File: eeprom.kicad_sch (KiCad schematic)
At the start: 2 parts, among them U8 CAT25320VI-GT3

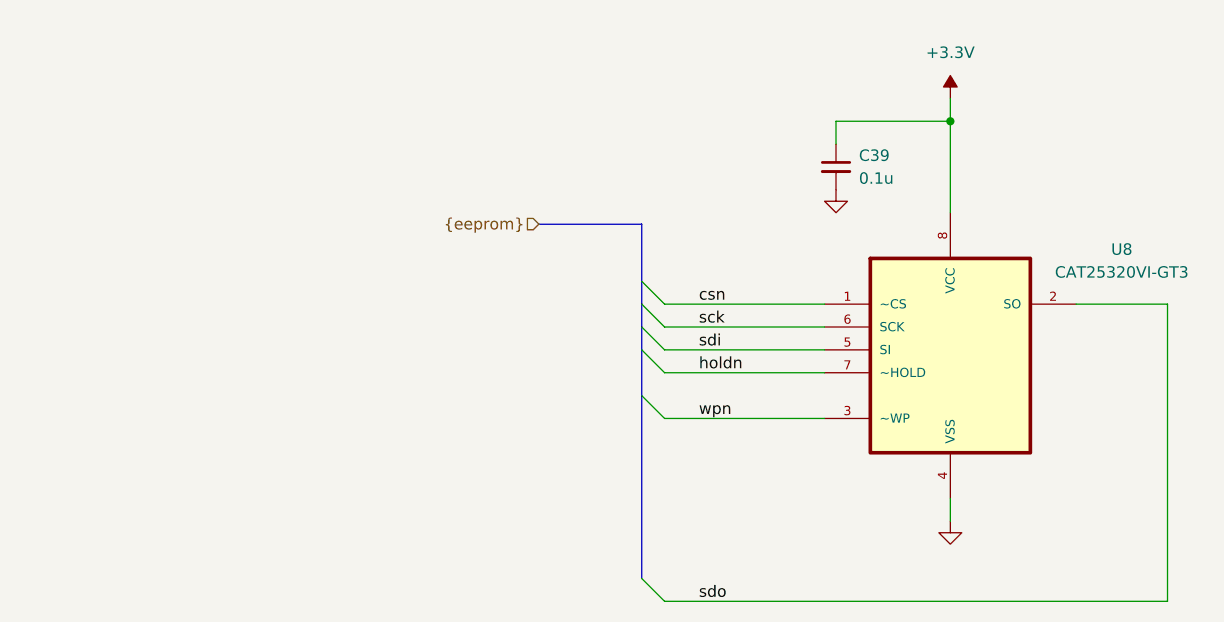
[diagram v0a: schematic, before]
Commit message: Add watchdog window IC
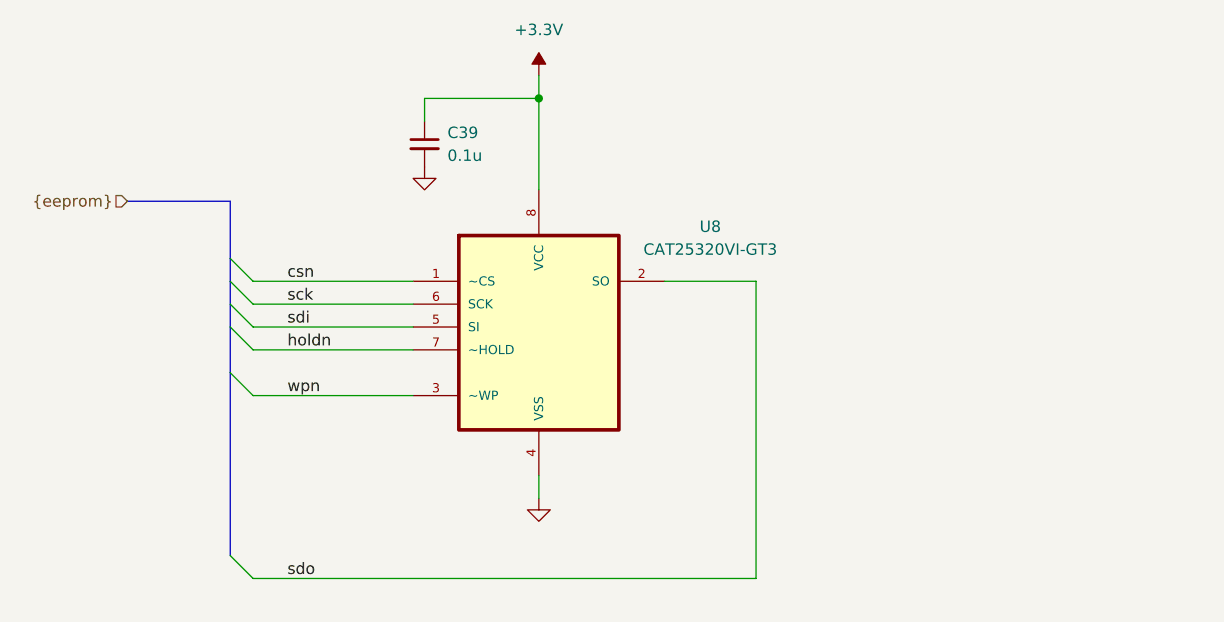
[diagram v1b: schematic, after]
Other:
- moved on the sheet: C39, U8

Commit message: Finish BOM
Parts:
- C39: Cost (none) -> .08; MFG (none) -> Taiyo-Yuden; MFG_PN (none) -> TMF212B7104KGHT
- U8: Cost (none) -> 0.55; MFG ON Semiconductor -> ON Semi
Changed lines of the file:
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@@
 			)
 		)
-		(property "Description" "CAT25320VI-GT3 EEPROM Memory, 32kbit, 40ns, 1.8 - 5.5 V 8-Pin SOIC | ON Semiconductor CAT25320VI-GT3"
+		(property "Description" "IC EEPROM 32KBIT SPI 10MHZ 8SOIC"
 			(at 91.948 65.786 0)
 			(effects
@@
 			)
 		)
-		(property "MFG" "ON Semiconductor"
+		(property "MFG" "ON Semi"
 			(at 93.472 61.214 0)
 			(effects
@@
 				)
 				(justify bottom)
+				(hide yes)
+			)
+		)
+		(property "MANUFACTURER_PART_NUMBER" ""
+			(at 91.44 87.63 0)
+			(effects
+				(font
+					(size 1.27 1.27)
+				)
+				(hide yes)
+			)
+		)
+		(property "MFR_NAME" ""
+			(at 91.44 87.63 0)
+			(effects
+				(font
+					(size 1.27 1.27)
+				)
+				(hide yes)
+			)
+		)
+		(property "Part" ""
+			(at 91.44 87.63 0)
+			(effects
+				(font
+					(size 1.27 1.27)
+				)
+				(hide yes)
+			)
+		)
+		(property "Tolerance" ""
+			(at 91.44 87.63 0)
+			(effects
+				(font
+					(size 1.27 1.27)
+				)
+				(hide yes)
+			)
+		)
+		(property "Type" ""
+			(at 91.44 87.63 0)
+			(effects
+				(font
+					(size 1.27 1.27)
+				)
+				(hide yes)
+			)
+		)
+		(property "VENDOR" ""
+			(at 91.44 87.63 0)
+			(effects
+				(font
+					(size 1.27 1.27)
+				)
+				(hide yes)
+			)
+		)
+		(property "Voltage" ""
+			(at 91.44 87.63 0)
+			(effects
+				(font
+					(size 1.27 1.27)
+				)
+				(hide yes)
+			)
+		)
+		(property "Cost" "0.55"
+			(at 91.44 87.63 0)
+			(effects
+				(font
+					(size 1.27 1.27)
+				)
 				(hide yes)
 			)
@@
 			)
 		)
-		(property "Description" "Unpolarized capacitor, small symbol"
-			(at 76.2 64.77 0)
-			(effects
+		(property "Description" "CAP CER 0.1UF 25V X7R 0805"
+			(at 76.2 64.77 0)
+			(effects
+				(font
+					(size 1.27 1.27)
+				)
+				(hide yes)
+			)
+		)
+		(property "MANUFACTURER_PART_NUMBER" ""
+			(at 76.2 64.77 0)
+			(effects
+				(font
+					(size 1.27 1.27)
+				)
+				(hide yes)
+			)
+		)
+		(property "MFR_NAME" ""
+			(at 76.2 64.77 0)
+			(effects
+				(font
+					(size 1.27 1.27)
+				)
+				(hide yes)
+			)
+		)
+		(property "Part" ""
+			(at 76.2 64.77 0)
+			(effects
+				(font
+					(size 1.27 1.27)
+				)
+				(hide yes)
+			)
+		)
+		(property "Tolerance" ""
+			(at 76.2 64.77 0)
+			(effects
+				(font
+					(size 1.27 1.27)
+				)
+				(hide yes)
+			)
+		)
+		(property "Type" ""
+			(at 76.2 64.77 0)
+			(effects
+				(font
+					(size 1.27 1.27)
+				)
+				(hide yes)
+			)
+		)
+		(property "VENDOR" ""
+			(at 76.2 64.77 0)
+			(effects
+				(font
+					(size 1.27 1.27)
+				)
+				(hide yes)
+			)
+		)
+		(property "Voltage" ""
+			(at 76.2 64.77 0)
+			(effects
+				(font
+					(size 1.27 1.27)
+				)
+				(hide yes)
+			)
+		)
+		(property "MFG" "Taiyo-Yuden"
+			(at 76.2 64.77 0)
+			(effects
+				(font
+					(size 1.27 1.27)
+				)
+				(hide yes)
+			)
+		)
+		(property "MFG_PN" "TMF212B7104KGHT"
+			(at 76.2 64.77 0)
+			(effects
+				(font
+					(size 1.27 1.27)
+				)
+				(hide yes)
+			)
+		)
+		(property "Cost" ".08"
+			(at 76.2 64.77 0)
+			(effects

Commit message: Nightly commit
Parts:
- C39: footprint Capacitor_SMD:C_0805_2012Metric -> My Footprints:C_0805_2012Metric
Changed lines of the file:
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@@
 			)
 		)
-		(property "Footprint" "Capacitor_SMD:C_0805_2012Metric"
+		(property "Footprint" "My Footprints:C_0805_2012Metric"
 			(at 76.2 64.77 0)
 			(effects
